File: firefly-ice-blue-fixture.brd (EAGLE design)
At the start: 36 x 100 mm, 16 parts, among them J1 CON-10, J2 CON-10

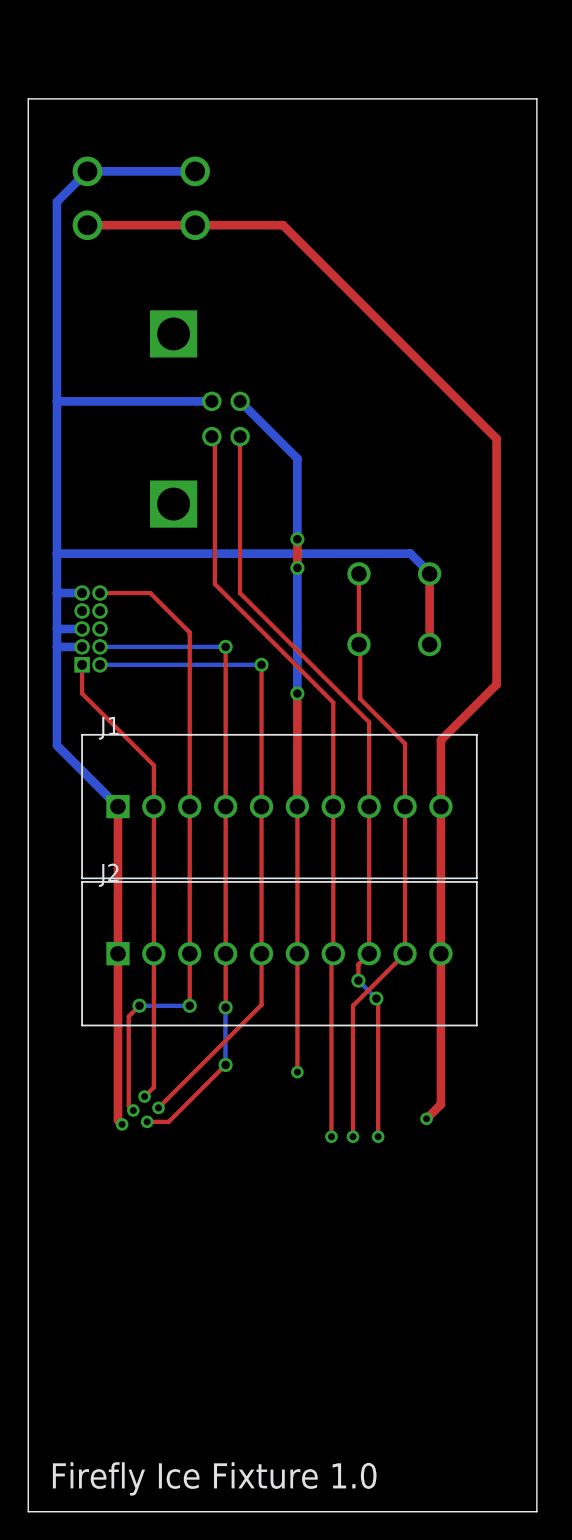
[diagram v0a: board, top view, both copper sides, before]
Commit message: increase size of test probe holes
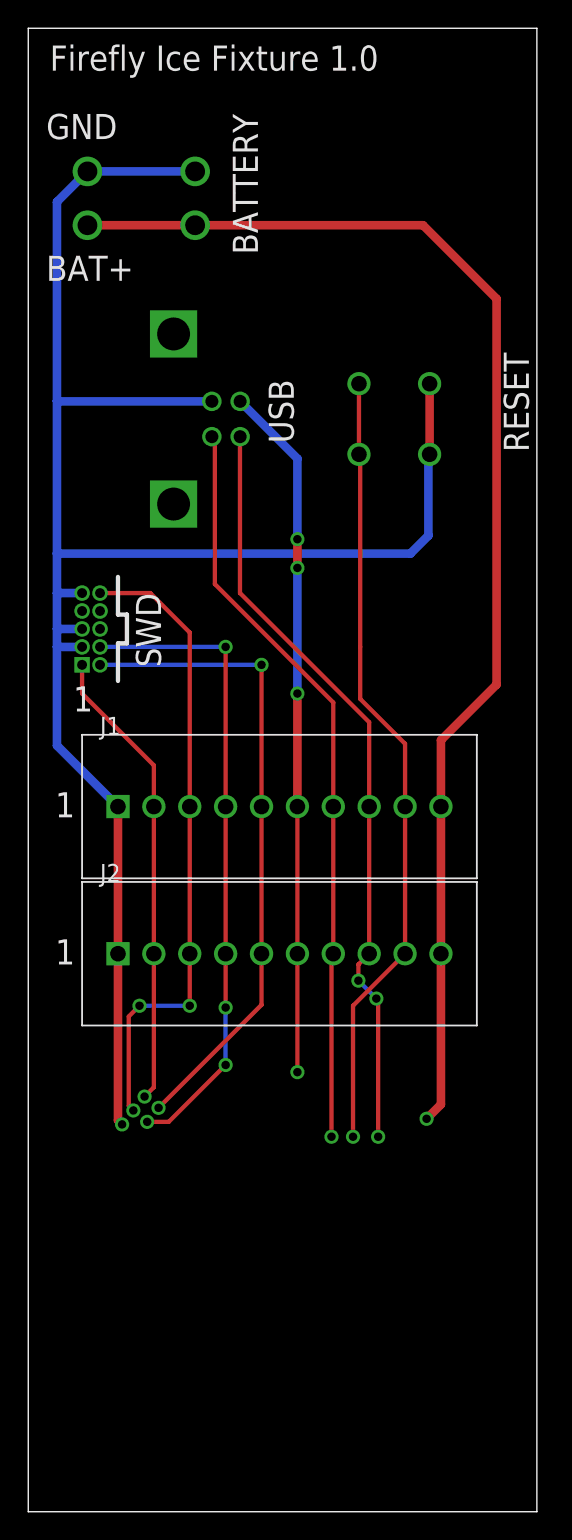
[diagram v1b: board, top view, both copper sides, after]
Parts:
- moved SRES 13.5 mm to (25.9, 77.3)
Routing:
- net USB_ID: track 42.7 -> 56.2 mm
- net BAT+: track 85.4 -> 91.2 mm
- net GND: track 126.2 -> 131.8 mm
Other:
- board size 36 x 100 mm -> 36 x 105 mm
- board text added: "1"
- board text added: "BAT+"
- board text added: "BATTERY"
- board text added: "GND"
- board text added: "RESET"
- board text added: "SWD"
- board text added: "USB"
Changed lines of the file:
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@@
 <plain>
 <wire x1="0" y1="0" x2="36" y2="0" width="0" layer="20"/>
-<wire x1="36" y1="0" x2="36" y2="100" width="0" layer="20"/>
-<wire x1="36" y1="100" x2="0" y2="100" width="0" layer="20"/>
-<wire x1="0" y1="100" x2="0" y2="0" width="0" layer="20"/>
-<text x="1.524" y="1.651" size="1.778" layer="111">Firefly Ice Fixture 1.0</text>
-<text x="34.163" y="1.651" size="1.778" layer="112" rot="MR0">Firefly Ice Fixture 1.0</text>
+<wire x1="36" y1="0" x2="36" y2="105" width="0" layer="20"/>
+<wire x1="36" y1="105" x2="0" y2="105" width="0" layer="20"/>
+<wire x1="0" y1="105" x2="0" y2="0" width="0" layer="20"/>
+<text x="1.524" y="102" size="1.778" layer="111">Firefly Ice Fixture 1.0</text>
+<text x="34.163" y="102" size="1.778" layer="112" rot="MR0">Firefly Ice Fixture 1.0</text>
+<text x="1.27" y="97.155" size="1.778" layer="111">GND</text>
+<text x="1.27" y="87.122" size="1.778" layer="111">BAT+</text>
+<text x="33.655" y="82.042" size="1.778" layer="111" rot="R270">RESET</text>
+<text x="17.018" y="80.137" size="1.778" layer="111" rot="R270">USB</text>
+<text x="14.478" y="98.933" size="1.778" layer="111" rot="R270">BATTERY</text>
+<text x="7.62" y="65.024" size="1.778" layer="111" rot="R270">SWD</text>
+<text x="3.175" y="56.642" size="1.778" layer="111">1</text>
+<text x="1.905" y="49.149" size="1.778" layer="111">1</text>
+<text x="1.905" y="38.735" size="1.778" layer="111">1</text>
+<wire x1="6.35" y1="66.167" x2="6.35" y2="63.5" width="0.3048" layer="111"/>
+<wire x1="6.35" y1="63.5" x2="6.985" y2="63.5" width="0.3048" layer="111"/>
+<wire x1="6.985" y1="63.5" x2="6.985" y2="61.468" width="0.3048" layer="111"/>
+<wire x1="6.985" y1="61.468" x2="6.35" y2="61.468" width="0.3048" layer="111"/>
+<wire x1="6.35" y1="61.468" x2="6.35" y2="58.801" width="0.3048" layer="111"/>
 </plain>
 <attributes>
@@
 <attribute name="ORDERING-CODE" value="USB-B1HSB6" x="10.287" y="77.343" size="1.778" layer="28" rot="MR90" display="off"/>
 </element>
-<element name="SRES" library="firefly" package="KS-01Q-01" value="SPST-NOKS-01Q-01" x="25.908" y="63.881" rot="MR0">
-<attribute name="MANUFACTURER" value="E-Switch" x="25.908" y="63.881" size="1.778" layer="28" rot="MR0" display="off"/>
-<attribute name="ORDERING-CODE" value="KS-01Q-01" x="25.908" y="63.881" size="1.778" layer="28" rot="MR0" display="off"/>
+<element name="SRES" library="firefly" package="KS-01Q-01" value="SPST-NOKS-01Q-01" x="25.908" y="77.343" rot="MR0">
+<attribute name="MANUFACTURER" value="E-Switch" x="25.908" y="77.343" size="1.778" layer="28" rot="MR0" display="off"/>
+<attribute name="ORDERING-CODE" value="KS-01Q-01" x="25.908" y="77.343" size="1.778" layer="28" rot="MR0" display="off"/>
 </element>
 <element name="JBAT" library="firefly" package="20020303-D021B01LF" value="CON-220020303-D021B01LF" x="8.001" y="92.964" rot="MR90">
@@
 <wire x1="12.997" y1="78.593" x2="2.052" y2="78.593" width="0.6096" layer="16"/>
 <wire x1="2.052" y1="78.593" x2="2.032" y2="78.613" width="0.6096" layer="16"/>
-<wire x1="28.408" y1="66.381" x2="28.408" y2="66.461" width="0.6096" layer="16"/>
-<wire x1="28.408" y1="66.461" x2="27.051" y2="67.818" width="0.6096" layer="16"/>
+<wire x1="28.321" y1="69.088" x2="27.051" y2="67.818" width="0.6096" layer="16"/>
 <wire x1="27.051" y1="67.818" x2="2.032" y2="67.818" width="0.6096" layer="16"/>
 <wire x1="3.81" y1="65.024" x2="2.032" y2="65.024" width="0.6096" layer="16"/>
 <wire x1="3.81" y1="62.484" x2="2.032" y2="62.484" width="0.6096" layer="16"/>
 <wire x1="3.81" y1="61.214" x2="2.032" y2="61.214" width="0.6096" layer="16"/>
-<wire x1="28.408" y1="66.381" x2="28.408" y2="61.381" width="0.6096" layer="1"/>
+<wire x1="28.321" y1="69.088" x2="28.321" y2="74.803" width="0.6096" layer="16"/>
+<wire x1="28.321" y1="74.803" x2="28.408" y2="74.843" width="0.6096" layer="16"/>
+<wire x1="28.408" y1="79.843" x2="28.408" y2="74.843" width="0.6096" layer="1"/>
 </signal>
 <signal name="VCC">
@@
 <wire x1="22.987" y1="35.814" x2="26.67" y2="39.497" width="0.3048" layer="1"/>
 <wire x1="26.67" y1="39.497" x2="26.67" y2="49.911" width="0.3048" layer="1"/>
-<wire x1="23.408" y1="66.381" x2="23.408" y2="61.381" width="0.3048" layer="1"/>
 <wire x1="26.67" y1="49.911" x2="26.67" y2="54.356" width="0.3048" layer="1"/>
 <wire x1="26.67" y1="54.356" x2="23.495" y2="57.531" width="0.3048" layer="1"/>
 <wire x1="23.495" y1="57.531" x2="23.495" y2="61.214" width="0.3048" layer="1"/>
-<wire x1="23.495" y1="61.214" x2="23.408" y2="61.381" width="0.3048" layer="1"/>
+<wire x1="23.495" y1="61.214" x2="23.495" y2="74.803" width="0.3048" layer="1"/>
+<wire x1="23.495" y1="74.803" x2="23.455" y2="74.843" width="0.3048" layer="1"/>
+<wire x1="23.455" y1="74.843" x2="23.408" y2="74.843" width="0.3048" layer="1"/>
+<wire x1="23.408" y1="79.843" x2="23.408" y2="74.843" width="0.3048" layer="1"/>
 </signal>
 <signal name="BAT+">
@@
 <wire x1="29.21" y1="49.911" x2="29.21" y2="54.61" width="0.6096" layer="1"/>
 <wire x1="29.21" y1="54.61" x2="33.147" y2="58.547" width="0.6096" layer="1"/>
-<wire x1="33.147" y1="58.547" x2="33.147" y2="75.946" width="0.6096" layer="1"/>
-<wire x1="33.147" y1="75.946" x2="18.034" y2="91.059" width="0.6096" layer="1"/>
-<wire x1="18.034" y1="91.059" x2="11.811" y2="91.059" width="0.6096" layer="1"/>
+<wire x1="33.147" y1="58.547" x2="33.147" y2="85.852" width="0.6096" layer="1"/>
+<wire x1="33.147" y1="85.852" x2="27.94" y2="91.059" width="0.6096" layer="1"/>
+<wire x1="27.94" y1="91.059" x2="11.811" y2="91.059" width="0.6096" layer="1"/>
 <wire x1="11.811" y1="91.059" x2="4.191" y2="91.059" width="0.6096" layer="1"/>
 </signal>
